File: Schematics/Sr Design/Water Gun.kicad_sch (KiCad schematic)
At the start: 8 parts, among them J1 Raspberry_Pi_4, Q1 C6144, Q2 C6144

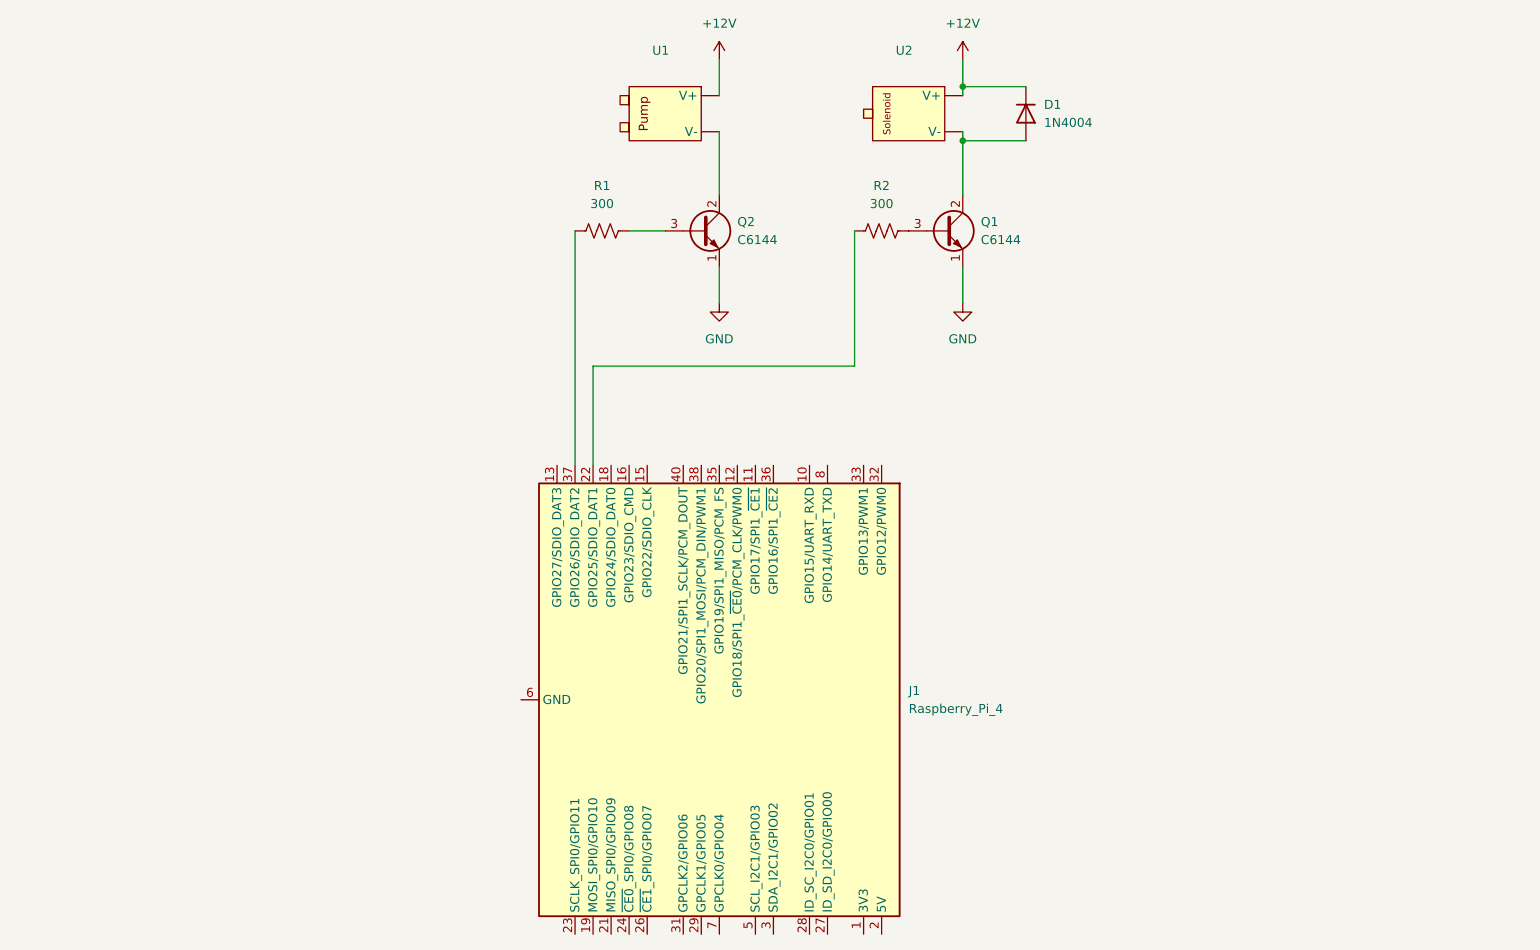
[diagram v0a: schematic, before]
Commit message: SCHM updated need to figure out how we want to apply our power design.
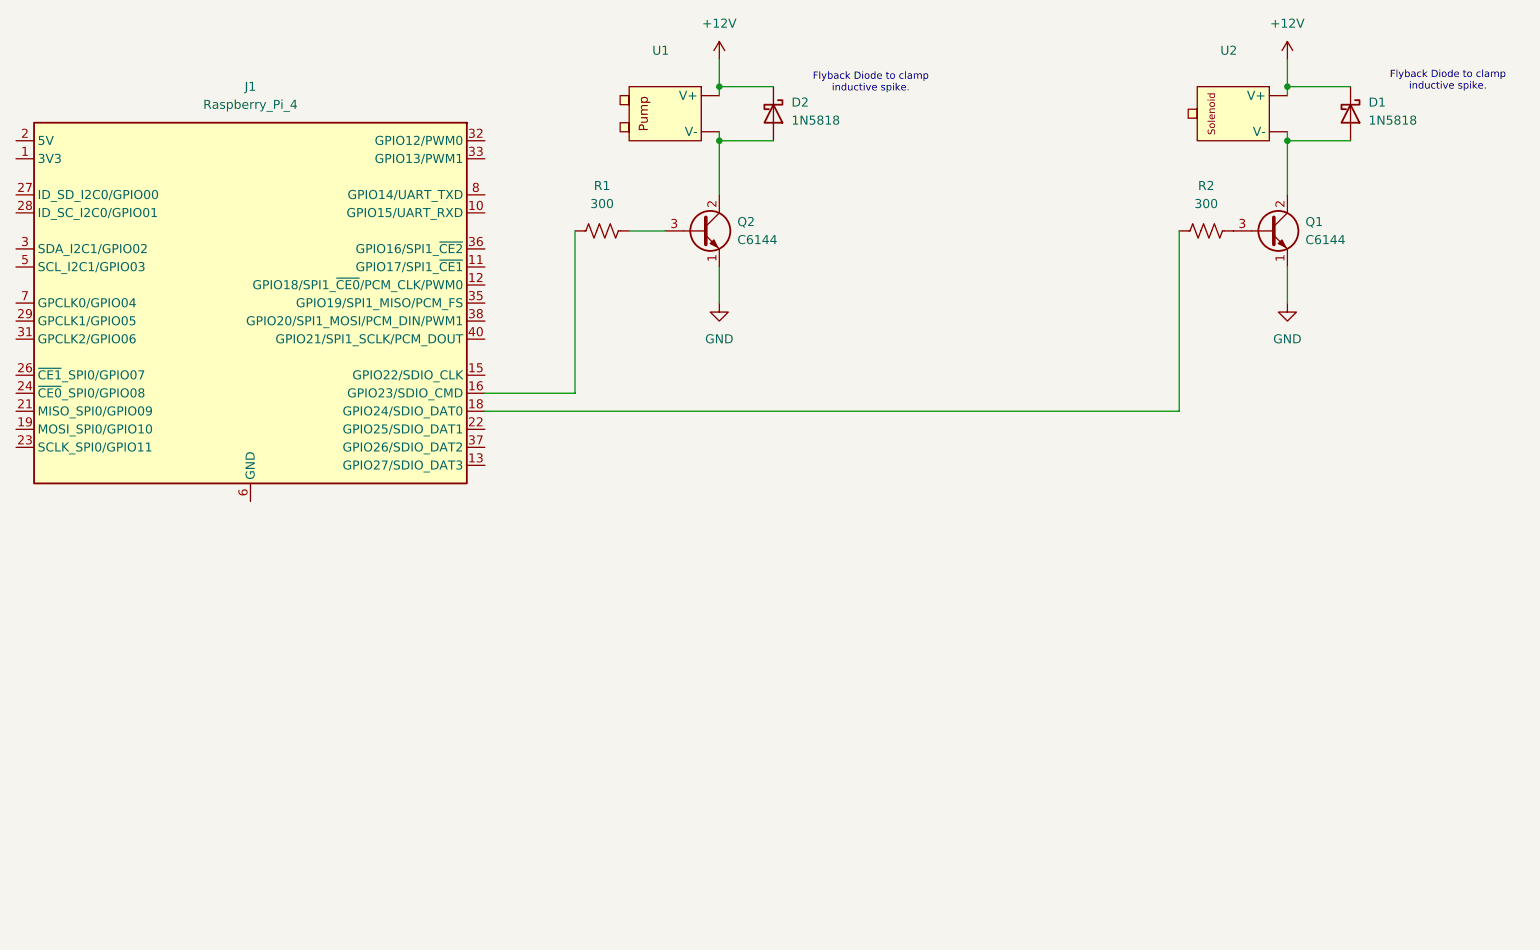
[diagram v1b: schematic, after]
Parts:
- removed D1: 1N4004, Diode_THT:D_DO-41_SOD81_P10.16mm_Horizontal, symbol Diode:1N4004
- added D1, D2: 1N5818, Diode_THT:D_DO-41_SOD81_P10.16mm_Horizontal, symbol Diode:1N5818
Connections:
- net +12V: now also D1.1 (K), D2.1 (K)
- net at R2.1: now also J1.18 (GPIO24/SDIO_DAT0); no longer J1.22 (GPIO25/SDIO_DAT1)
- net at Q2.2 (C), U1. (V-): now also D2.2 (A)
- net at Q1.2 (C), U2. (V-): now also D1.2 (A)
- net at J1.16 (GPIO23/SDIO_CMD): now also R1.1
- net at J1.37 (GPIO26/SDIO_DAT2): no longer R1.1
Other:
- note added: "Flyback Diode to clamp inductive spike."
- title: (none) -> Water Gun
- moved on the sheet: J1, Q1, R2, U2
